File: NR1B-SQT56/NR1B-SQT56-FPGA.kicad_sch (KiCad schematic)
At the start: 44 parts, among them J3 Conn_01x07, J4 Conn_02x10_Odd_Even, J5 Conn_02x10_Odd_Even, J6 Conn_02x10_Odd_Even, SW1 SW_Push, U7 W25Q128JVS, U8 Lattice_HX1K-CB132, Y1 SiT1602B, Y2 SiT2001

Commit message: Finish NR1B-SQT56
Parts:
- removed C20, C26: 0.1uF, Capacitor_SMD:C_0805_2012Metric, symbol Device:C
- removed D20, D21, D22, D23, D24, D25, D26, D27, D28, D29: ESDA6V1BC6, Package_TO_SOT_SMD:SOT-23-6, symbol NISoC-Socket:ESDA6V1BC6
- removed J4: Conn_02x10_Odd_Even, symbol Connector_Generic:Conn_02x10_Odd_Even
- removed U8: Lattice_HX1K-CB132, NISoC-Socket:Lattice_CB132-iCE, symbol NISoC-Socket:Lattice_HX1K-CB132
- removed Y1: SiT1602B, NISoC-Socket:SiTime_1602B_2.5x2.0mm_4pin, symbol NISoC-Socket:SiT1602B
- added C12: 10uF, Capacitor_SMD:C_0805_2012Metric, symbol Device:C_Polarized
- added C14, C17: 0.1uF, Capacitor_SMD:C_0603_1608Metric, symbol Device:C
- added D19: GREEN, LED_SMD:LED_0805_2012Metric, symbol Device:LED
- added D21, D22, D23, D24, D27, D28: PESD4USB3B_TBS, Package_DFN_QFN:Diodes_UDFN-10_1.0x2.5mm_P0.5mm, symbol NISoC-Socket:PESD4USB3B_TBS
- added R6: 100, Resistor_SMD:R_0603_1608Metric, symbol Device:R
- added R7, R9: 10k, Resistor_SMD:R_0603_1608Metric, symbol Device:R
- added TP10: IOR_109, TestPoint:TestPoint_THTPad_D1.5mm_Drill0.7mm, symbol Connector:TestPoint
- added TP11: IOT_188, TestPoint:TestPoint_THTPad_D1.5mm_Drill0.7mm, symbol Connector:TestPoint
- added TP9: CDONE, TestPoint:TestPoint_2Pads_Pitch2.54mm_Drill0.8mm, symbol Connector:TestPoint_2Pole
- added U7: Lattice_HX8K-CB132, NISoC-Socket:Lattice_CB132-iCE, symbol NISoC-Socket:Lattice_HX8K-CB132
- C11: renamed from C4; footprint (none) -> Capacitor_SMD:C_0805_2012Metric
- C13: renamed from C5; footprint Capacitor_SMD:C_0805_2012Metric -> Capacitor_SMD:C_0603_1608Metric
- C15: renamed from C2; footprint Capacitor_SMD:C_0805_2012Metric -> Capacitor_SMD:C_0603_1608Metric
- C16: renamed from C3; footprint Capacitor_SMD:C_0805_2012Metric -> Capacitor_SMD:C_0603_1608Metric
- C18: renamed from C6; footprint Capacitor_SMD:C_0805_2012Metric -> Capacitor_SMD:C_0402_1005Metric
- C19: renamed from C9; footprint Capacitor_SMD:C_0805_2012Metric -> Capacitor_SMD:C_0402_1005Metric
- C20: renamed from C7; footprint Capacitor_SMD:C_0805_2012Metric -> Capacitor_SMD:C_0402_1005Metric
- C21: renamed from C12; footprint Capacitor_SMD:C_0805_2012Metric -> Capacitor_SMD:C_0402_1005Metric
- C22: renamed from C11; footprint Capacitor_SMD:C_0805_2012Metric -> Capacitor_SMD:C_0402_1005Metric
- C23: renamed from C15; footprint Capacitor_SMD:C_0805_2012Metric -> Capacitor_SMD:C_0402_1005Metric
- C24: renamed from C13; footprint Capacitor_SMD:C_0805_2012Metric -> Capacitor_SMD:C_0402_1005Metric
- C25: renamed from C18; footprint Capacitor_SMD:C_0805_2012Metric -> Capacitor_SMD:C_0402_1005Metric
- C26: renamed from C17; footprint Capacitor_SMD:C_0805_2012Metric -> Capacitor_SMD:C_0402_1005Metric
- C27: renamed from C21; footprint Capacitor_SMD:C_0805_2012Metric -> Capacitor_SMD:C_0402_1005Metric
- C28: renamed from C27; footprint Capacitor_SMD:C_0805_2012Metric -> Capacitor_SMD:C_0402_1005Metric
- C29: renamed from C28; footprint Capacitor_SMD:C_0805_2012Metric -> Capacitor_SMD:C_0402_1005Metric
- C30: renamed from C29; footprint Capacitor_SMD:C_0805_2012Metric -> Capacitor_SMD:C_0402_1005Metric
- D20: renamed from D19; footprint (none) -> Diode_SMD:D_SOD-323
- J3: footprint Connector_PinHeader_1.27mm:PinHeader_1x07_P1.27mm_Vertical -> Connector_PinHeader_2.54mm:PinHeader_1x07_P2.54mm_Vertical
- J4: renamed from J5; footprint (none) -> Connector_PinHeader_2.54mm:PinHeader_2x10_P2.54mm_Vertical
- J5: renamed from J6; footprint (none) -> Connector_PinHeader_2.54mm:PinHeader_2x10_P2.54mm_Vertical
- JP1: value Jumper_2_Open -> 0.1" Header; footprint (none) -> Connector_PinHeader_2.54mm:PinHeader_1x02_P2.54mm_Vertical
- R10: renamed from R6; footprint (none) -> Resistor_SMD:R_0603_1608Metric
- R11: renamed from R8; footprint (none) -> Resistor_SMD:R_0603_1608Metric
- R5: renamed from R7; footprint (none) -> Resistor_SMD:R_0603_1608Metric
- R8: renamed from R5; footprint (none) -> Resistor_SMD:R_0603_1608Metric
- SW1: value SW_Push -> Push Button; footprint (none) -> NISoC-Socket:TE_1-1571636-0
- renumbered U7 to U8, Y2 to Y1
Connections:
- net IOL_11A is gone; now on net GND: J5.3 (Pin_3)
- net IOL_11B is gone; now on net GND: J5.4 (Pin_4)
- net IOL_9A is gone; now on net GND: J5.1 (Pin_1)
- net IOL_9B is gone; now on net GND: J5.2 (Pin_2)
- net +1V2: now also R6.1, U7.F8 (VCC), U7.G6 (VCC), U7.H9 (VCC), U7.J4 (VCC), U7.J7 (VCC)
- net +3.3V: now also J5.19 (Pin_19), J5.20 (Pin_20), U7.A14 (VPP_2V5), U7.A8 (VCCIO_0), U7.E3 (VCCIO_3), U7.F6 (VCCIO_0), U7.F9 (VCCIO_1), U7.H14 (VCCIO_1), U7.J6 (VCCIO_3), U7.J9 (VCCIO_2), U7.K1 (VCCIO_3), U7.L11 (VCC_SPI), U7.M5 (VCCIO_2); no longer Y1.4 (VDD)
- net A0: now also U7.G11 (IOR_136)
- net A1: now also U7.A7 (IOT_197_GBIN1)
- net A10: now also U7.A5 (IOT_208)
- net A11: now also U7.C12 (IOT_172)
- net A12: now also U7.B1 (IOL_2A)
- net A13: now also U7.A4 (IOT_219)
- net A14: now also U7.D11 (IOT_178)
- net A15: now also U7.C1 (IOL_2B)
- net A16: now also U7.B14 (IOR_161)
- net A17: now also U7.C10 (IOT_186)
- net A18: now also U7.D6 (IOT_207)
- net A19: now also U7.A6 (IOT_198_GBIN0)
- net A2: now also U7.A10 (IOT_181)
- net A20: now also U7.C5 (IOT_212)
- net A21: now also U7.C4 (IOT_221)
- net A22: now also U7.A3 (IOT_222)
- net A23: now also U7.A12 (IOT_170)
- net A24: now also U7.H11 (IOR_128)
- net A25: now also U7.F11 (IOR_144)
- net A3: now also U7.A2 (IOT_223)
- net A4: now also U7.C6 (IOT_206)
- net A5: now also U7.A11 (IOT_179)
- net A6: now also U7.A1 (IOT_225)
- net A7: now also U7.D7 (IOT_202)
- net A8: now also U7.C11 (IOT_174)
- net A9: now also U7.D5 (IOT_211)
- net CDONE: now also R7.2, R9.2, TP9.2, U7.M10 (CDONE)
- net CTRL.~{BYTE}: now also U7.K14 (IOR_117)
- net CTRL.~{CE}: now also U7.K11 (IOR_116)
- net CTRL.~{OE}: now also U7.G12 (IOR_129)
- net CTRL.~{WE}: now also U7.D10 (IOT_177)
- net DQ0: now also U7.K12 (IOR_115)
- net DQ1: now also U7.H12 (IOR_120)
- net DQ10: now also U7.G14 (IOR_141_GBIN2)
- net DQ11: now also U7.C14 (IOR_154)
- net DQ12: now also U7.E12 (IOR_147)
- net DQ13: now also U7.P14 (IOR_110)
- net DQ14: now also U7.F12 (IOR_137)
- net DQ15: now also U7.D12 (IOR_160)
- net DQ2: now also U7.D14 (IOR_152)
- net DQ3: now also U7.L14 (IOR_114)
- net DQ4: now also U7.N14 (IOR_112)
- net DQ5: now also U7.F14 (IOR_140_GBIN3)
- net DQ6: now also U7.E11 (IOR_146)
- net DQ7: now also U7.J12 (IOR_118)
- net DQ8: now also U7.E14 (IOR_148)
- net DQ9: now also U7.L12 (IOR_111)
- net FLASH.DI_IO0: now also U7.P11 (IOB_106_SDI)
- net FLASH.DO_IO1: now also U7.M11 (IOB_105_SDO)
- net FLASH.SCK: now also U7.P13 (IOB_108_SS)
- net FLASH.~{CS}: now also U7.P12 (IOB_107_SCK)
- net FPGA_CLK: now also U7.P7 (IOB_81_GBIN5)
- net GND: now also SW1.3, C17.2, D19.1 (K), D21.3 (C), D21.8 (C), D22.3 (C), D22.8 (C), D23.3 (C), D23.8 (C), D24.3 (C), D24.8 (C), D27.3 (C), D27.8 (C), D28.3 (C), D28.8 (C), TP9.1, U7.A9 (GND), U7.F1 (GND), U7.F7 (GND), U7.G7 (GND), U7.G8 (GND), U7.G9 (GND), U7.H6 (GND), U7.H7 (GND), U7.H8 (GND), U7.J14 (GND), U7.J8 (GND), U7.L3 (GND), U7.P6 (GND); no longer J5.10 (Pin_10), J5.13 (Pin_13), J5.14 (Pin_14), J5.17 (Pin_17), J5.18 (Pin_18), J5.19 (Pin_19), J5.20 (Pin_20), J5.9 (Pin_9)
- net QSPI.IO0: now also U7.M3 (IOB_64)
- net QSPI.IO1: now also U7.M4 (IOB_63)
- net QSPI.IO2: now also U7.P3 (IOB_59)
- net QSPI.IO3: now also U7.P2 (IOB_56)
- net QSPI.SCK: now also U7.L5 (IOB_71)
- net QSPI.~{CS}: now also U7.L4 (IOB_72)
- net RY/~{BY}: now also U7.C7 (IOT_200)
- net VCCPLL0: now reaches C11.1, C13.1, R5.2
- net VCCPLL0: now also U7.M8 (VCCPLL0)
- net GNDPLL0: now reaches C11.2, C13.2
- net GNDPLL0: now also U7.L7 (GNDPLL0)
- net ~{CRESET}: now reaches D20.2 (A), JP1.2 (B), R11.1, SW1.2
- net ~{CRESET}: now also C17.1, U7.L10 (~{CRESET})
- net CLK_VDD: now reaches C15.2, R8.2
- net CLK_VDD: now also Y1.4 (VDD)
- net IOL_12A renamed IOB_104_CBSEL1
- net IOB_104_CBSEL1: now also D27.1, D27.10, U7.P10 (IOB_104_CBSEL1)
- net IOL_12B renamed IOB_103_CBSEL0
- net IOB_103_CBSEL0: now also D27.2, D27.9, U7.L9 (IOB_103_CBSEL0)
- net IOL_1A renamed IOL_5-
- net IOL_5-: now also D21.2, D21.9, U7.E1 (IOL_5B)
- net IOL_1B renamed IOL_5+
- net IOL_5+: now also D21.1, D21.10, U7.D1 (IOL_5A)
- net IOL_2A renamed IOL_9-
- net IOL_9-: now also D21.5, D21.6, U7.F3 (IOL_9B)
- net IOL_2B renamed IOL_9+
- net IOL_9+: now also D21.4, D21.7, U7.F4 (IOL_9A)
- net IOL_3A renamed IOL_13-
- net IOL_13-: now also D22.2, D22.9, U7.G1 (IOL_13B_GBIN7)
- net IOL_3B renamed IOL_13+
- net IOL_13+: now also D22.1, D22.10, U7.G3 (IOL_13A)
- net IOL_4A renamed IOL_14-
- net IOL_14-: now also D22.5, D22.6, U7.H3 (IOL_14B)
- net IOL_4B renamed IOL_14+
- net IOL_14+: now also D22.4, D22.7, U7.H1 (IOL_14A_GBIN6)
- net IOL_5A renamed IOL_12-
- net IOL_12-: now also D23.2, D23.9, U7.J1 (IOL_12B)
- net IOL_5B renamed IOL_12+
- net IOL_12+: now also D23.1, D23.10, U7.J3 (IOL_12A)
- net IOL_6A renamed IOL_18-
- net IOL_18-: now also D23.5, D23.6, U7.K4 (IOL_18B)
- net IOL_6B renamed IOL_18+
- net IOL_18+: now also D23.4, D23.7, U7.K3 (IOL_18A)
- net IOL_7A renamed IOL_23-
- net IOL_23-: now also D24.2, D24.9, U7.M1 (IOL_23B)
- net IOL_7B renamed IOL_23+
- net IOL_23+: now also D24.1, D24.10, U7.L1 (IOL_23A)
- net IOL_8A renamed IOL_25-
- net IOL_25-: now also D24.5, D24.6, U7.P1 (IOL_25B)
- net IOL_8B renamed IOL_25+
- net IOL_25+: now also D24.4, D24.7, U7.N1 (IOL_25A)
- new net: D19.2 (A), R7.1, R9.1
- new net GNDPLL1: C12.2, C14.2, U7.D8 (GNDPLL1)
- new net IOB_73: D28.5, D28.6, J5.17 (Pin_17), U7.P4 (IOB_73)
- new net IOB_74: D28.4, D28.7, J5.18 (Pin_18), U7.P5 (IOB_74)
- new net IOB_82_GBIN4: D27.5, D27.6, J5.9 (Pin_9), U7.P8 (IOB_82_GBIN4)
- new net IOB_87: D28.2, D28.9, J5.14 (Pin_14), U7.L8 (IOB_87)
- new net IOB_89: D27.4, D27.7, J5.10 (Pin_10), U7.P9 (IOB_89)
- new net IOB_91: D28.1, D28.10, J5.13 (Pin_13), U7.M9 (IOB_91)
- new net IOR_109: TP10.1, U7.M12 (IOR_109)
- new net IOT_188: TP11.1, U7.D9 (IOT_188)
- new net VCCPLL1: C12.1, C14.1, R6.2, U7.C8 (VCCPLL1)
- no-connect marks 4 -> 12
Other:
- note added: "Can also use SiT1602B"
- note added: "Clock"
- note added: "Configuration Flash"
- note added: "Diff. IO Breakout 1"
- note added: "Diff. IO Breakout 2"
- note added: "Diff. Pairs broken out for differential bus experimentation"
- note added: "FPGA Configuration Flash Program externally"
- note added: "FPGA Power and Configuration"
- note added: "Resets: Momentary: SW1 Persistent: JP1 Automatic: ~{EXT_RESET} through D19"
- note added: "Spare IO Breakout"
- note removed: "Address Bank"
- note removed: "Alternates--place only one."
- note removed: "Data/Control Bank"
- note removed: "Management"
- note removed: "Resets: Momentary: SW? Persistent: JP? Automatic: ~{EXT_RESET} through D?"
- note removed: "TODO: - CDONE LED - Test points - Status LEDs?"
- moved on the sheet: C11, C13, C15, C16, C18, C19, C20, C21, C22, C23, C24, C25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

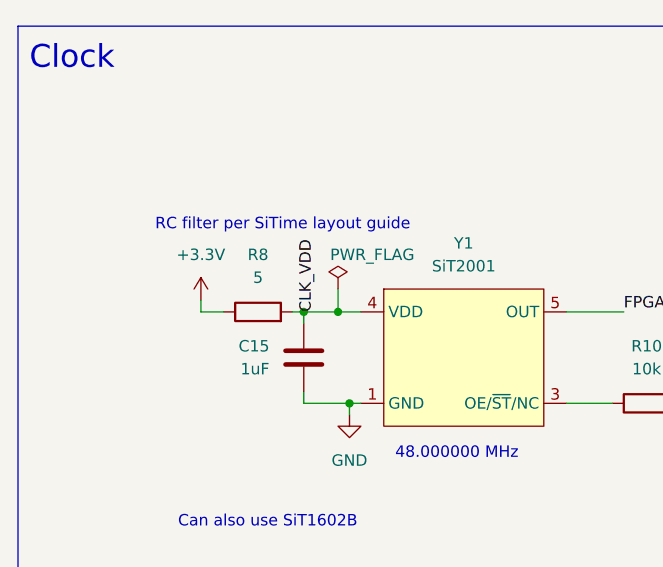
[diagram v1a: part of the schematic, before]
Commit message: Updated R8 to be 5.1 ohm
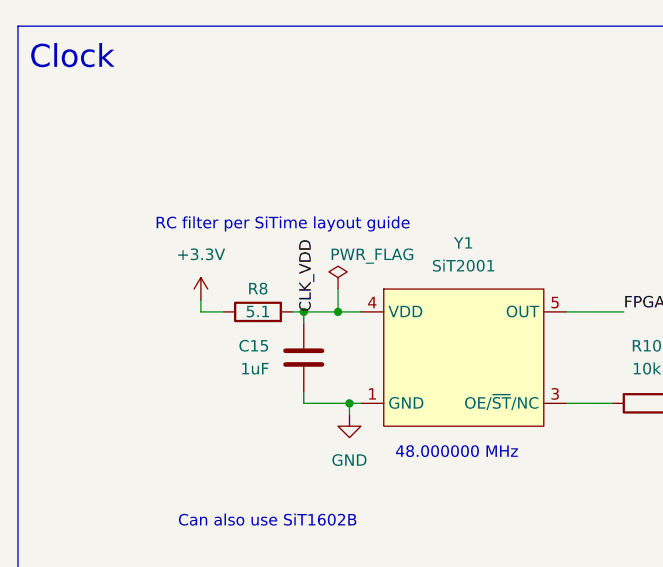
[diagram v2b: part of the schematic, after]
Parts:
- R8: value 5 -> 5.1
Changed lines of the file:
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@@
   )
   (symbol (lib_id "Device:R") (at 43.18 128.27 90) (unit 1)
-    (in_bom yes) (on_board yes) (fields_autoplaced)
-    (property "Reference" "R8" (id 0) (at 43.18 121.92 90))
-    (property "Value" "5" (id 1) (at 43.18 124.46 90))
+    (in_bom yes) (on_board yes)
+    (property "Reference" "R8" (id 0) (at 43.18 125.73 90))
+    (property "Value" "5.1" (id 1) (at 43.18 128.27 90))
     (property "Footprint" "Resistor_SMD:R_0603_1608Metric" (id 2) (at 43.18 130.048 90)
       (effects (font (size 1.27 1.27)) hide)
